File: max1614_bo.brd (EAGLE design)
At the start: 14 x 10.2 mm, 4 parts, among them IC1 MAX1614

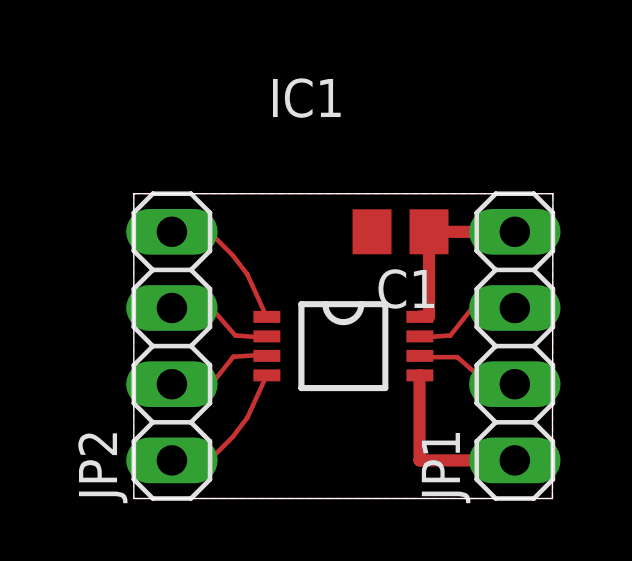
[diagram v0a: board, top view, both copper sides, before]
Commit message: move the dimension a bit, now if you make the mistake of printing it out for etching it will short the pins...
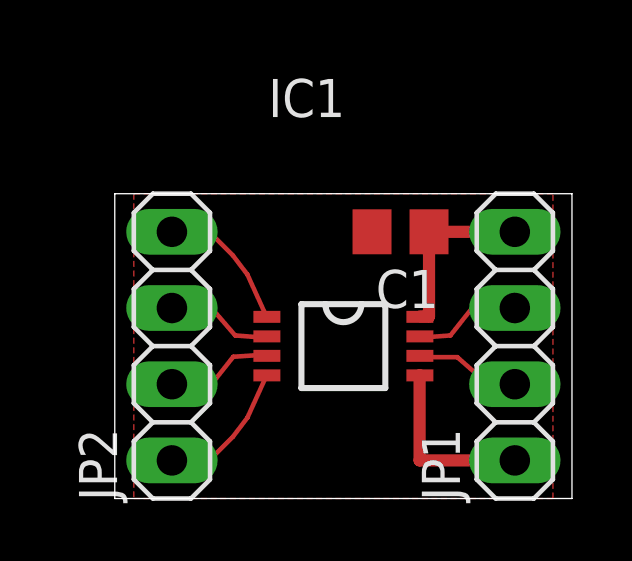
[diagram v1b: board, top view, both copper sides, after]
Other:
- board size 14 x 10.2 mm -> 15.2 x 10.2 mm
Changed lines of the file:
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@@
 <setting verticaltext="up"/>
 </settings>
-<grid distance="2.5" unitdist="mil" unit="mil" style="lines" multiple="1" display="yes" altdistance="0.025" altunitdist="inch" altunit="mil"/>
+<grid distance="25" unitdist="mil" unit="mil" style="lines" multiple="1" display="yes" altdistance="0.025" altunitdist="inch" altunit="mil"/>
 <layers>
 <layer number="1" name="Top" color="4" fill="1" visible="yes" active="yes"/>
@@
 <layer number="27" name="tValues" color="7" fill="1" visible="yes" active="yes"/>
 <layer number="28" name="bValues" color="7" fill="1" visible="yes" active="yes"/>
-<layer number="29" name="tStop" color="7" fill="3" visible="no" active="yes"/>
-<layer number="30" name="bStop" color="7" fill="6" visible="no" active="yes"/>
-<layer number="31" name="tCream" color="7" fill="4" visible="no" active="yes"/>
-<layer number="32" name="bCream" color="7" fill="5" visible="no" active="yes"/>
-<layer number="33" name="tFinish" color="6" fill="3" visible="no" active="yes"/>
-<layer number="34" name="bFinish" color="6" fill="6" visible="no" active="yes"/>
-<layer number="35" name="tGlue" color="7" fill="4" visible="no" active="yes"/>
-<layer number="36" name="bGlue" color="7" fill="5" visible="no" active="yes"/>
-<layer number="37" name="tTest" color="7" fill="1" visible="no" active="yes"/>
-<layer number="38" name="bTest" color="7" fill="1" visible="no" active="yes"/>
+<layer number="29" name="tStop" color="7" fill="3" visible="yes" active="yes"/>
+<layer number="30" name="bStop" color="7" fill="6" visible="yes" active="yes"/>
+<layer number="31" name="tCream" color="7" fill="4" visible="yes" active="yes"/>
+<layer number="32" name="bCream" color="7" fill="5" visible="yes" active="yes"/>
+<layer number="33" name="tFinish" color="6" fill="3" visible="yes" active="yes"/>
+<layer number="34" name="bFinish" color="6" fill="6" visible="yes" active="yes"/>
+<layer number="35" name="tGlue" color="7" fill="4" visible="yes" active="yes"/>
+<layer number="36" name="bGlue" color="7" fill="5" visible="yes" active="yes"/>
+<layer number="37" name="tTest" color="7" fill="1" visible="yes" active="yes"/>
+<layer number="38" name="bTest" color="7" fill="1" visible="yes" active="yes"/>
 <layer number="39" name="tKeepout" color="4" fill="11" visible="yes" active="yes"/>
 <layer number="40" name="bKeepout" color="1" fill="11" visible="yes" active="yes"/>
@@
 <layer number="42" name="bRestrict" color="1" fill="10" visible="yes" active="yes"/>
 <layer number="43" name="vRestrict" color="2" fill="10" visible="yes" active="yes"/>
-<layer number="44" name="Drills" color="7" fill="1" visible="no" active="yes"/>
-<layer number="45" name="Holes" color="7" fill="1" visible="no" active="yes"/>
-<layer number="46" name="Milling" color="3" fill="1" visible="no" active="yes"/>
-<layer number="47" name="Measures" color="7" fill="1" visible="no" active="yes"/>
+<layer number="44" name="Drills" color="7" fill="1" visible="yes" active="yes"/>
+<layer number="45" name="Holes" color="7" fill="1" visible="yes" active="yes"/>
+<layer number="46" name="Milling" color="3" fill="1" visible="yes" active="yes"/>
+<layer number="47" name="Measures" color="7" fill="1" visible="yes" active="yes"/>
 <layer number="48" name="Document" color="7" fill="1" visible="yes" active="yes"/>
 <layer number="49" name="Reference" color="7" fill="1" visible="yes" active="yes"/>
@@
 <board>
 <plain>
-<wire x1="0" y1="0" x2="13.95" y2="0" width="0" layer="20"/>
-<wire x1="13.95" y1="0" x2="13.97" y2="10.16" width="0" layer="20"/>
-<wire x1="13.97" y1="10.16" x2="0" y2="10.16" width="0" layer="20"/>
-<wire x1="0" y1="10.16" x2="0" y2="0" width="0" layer="20"/>
+<wire x1="-0.635" y1="0" x2="14.605" y2="0" width="0" layer="20"/>
+<wire x1="14.605" y1="0" x2="14.605" y2="10.16" width="0" layer="20"/>
+<wire x1="14.605" y1="10.16" x2="-0.635" y2="10.16" width="0" layer="20"/>
+<wire x1="-0.635" y1="10.16" x2="-0.635" y2="0" width="0" layer="20"/>
 </plain>
 <attributes>
